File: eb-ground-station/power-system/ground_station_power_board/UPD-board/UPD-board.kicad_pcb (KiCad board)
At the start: 2 copper layers, 140.7 x 86.5 mm, 171 parts, among them J1 Conn_01x04, J10 PI 1827486, J2 PC 1720806, J3 Conn_01x03, J4 Conn_01x03, J5 Conn_01x03, J6 Conn_01x03, J7 PI 1924143, J8 PI 1827923, J9 PI 1827486, Q1 DMN61D8L-LVT, Q10 DMN61D8L-LVT, Q11 SUD50P08-25L-E3, Q12 SUD50P08-25L-E3, Q13 DMN61D8L-LVT, Q14 DMN61D8L-LVT, Q15 DMN61D8L-LVT, Q16 SUD50P08-25L-E3, Q17 SUD50P08-25L-E3, Q18 DMN61D8L-LVT, Q19 SUD50P08-25L-E3, Q2 DMN61D8L-LVT, Q20 SUD50P08-25L-E3, Q21 SUD50P08-25L-E3, Q22 SUD50P08-25L-E3, Q3 DMN61D8L-LVT, Q4 SUD50P08-25L-E3, Q5 SUD50P08-25L-E3, Q6 DMN61D8L-LVT, Q7 DMN61D8L-LVT, Q8 DMN61D8L-LVT, Q9 DMN61D8L-LVT, U1 MAX7310ATE, U10 TC4427, U11 TC4427, U12 TC4427, U13 TC4427, U14 TC4427, U15 TC4427, U16 TC4427, U17 TC4427, U18 TC4427, U19 TC4427, U2 MAX7310ATE, U3 MAX7310ATE, U4 MCP9808, U5 ADS1115IDGS, U6 UA78M33, U7 U_RasPi_40pin, U8 TC4427, U9 TC4427

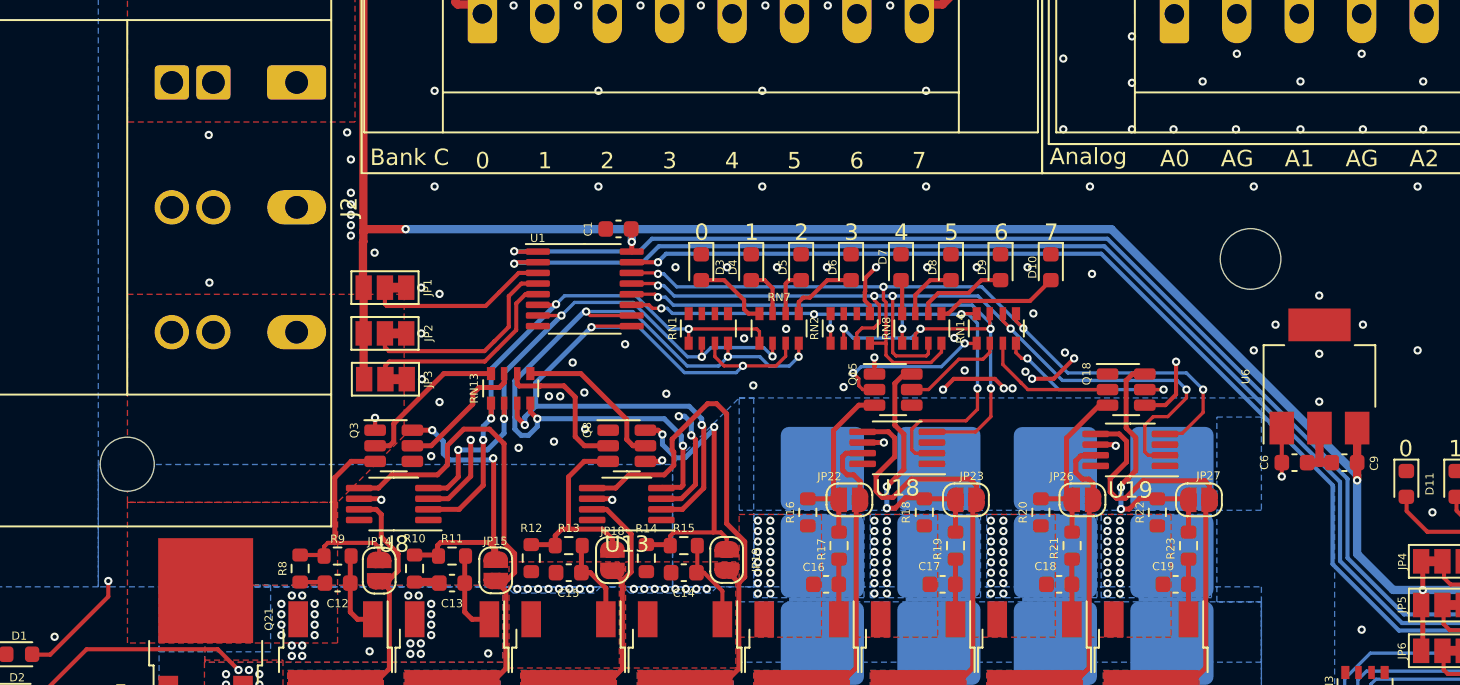
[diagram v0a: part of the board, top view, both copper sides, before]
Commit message: Upgrading Bank A to 16A
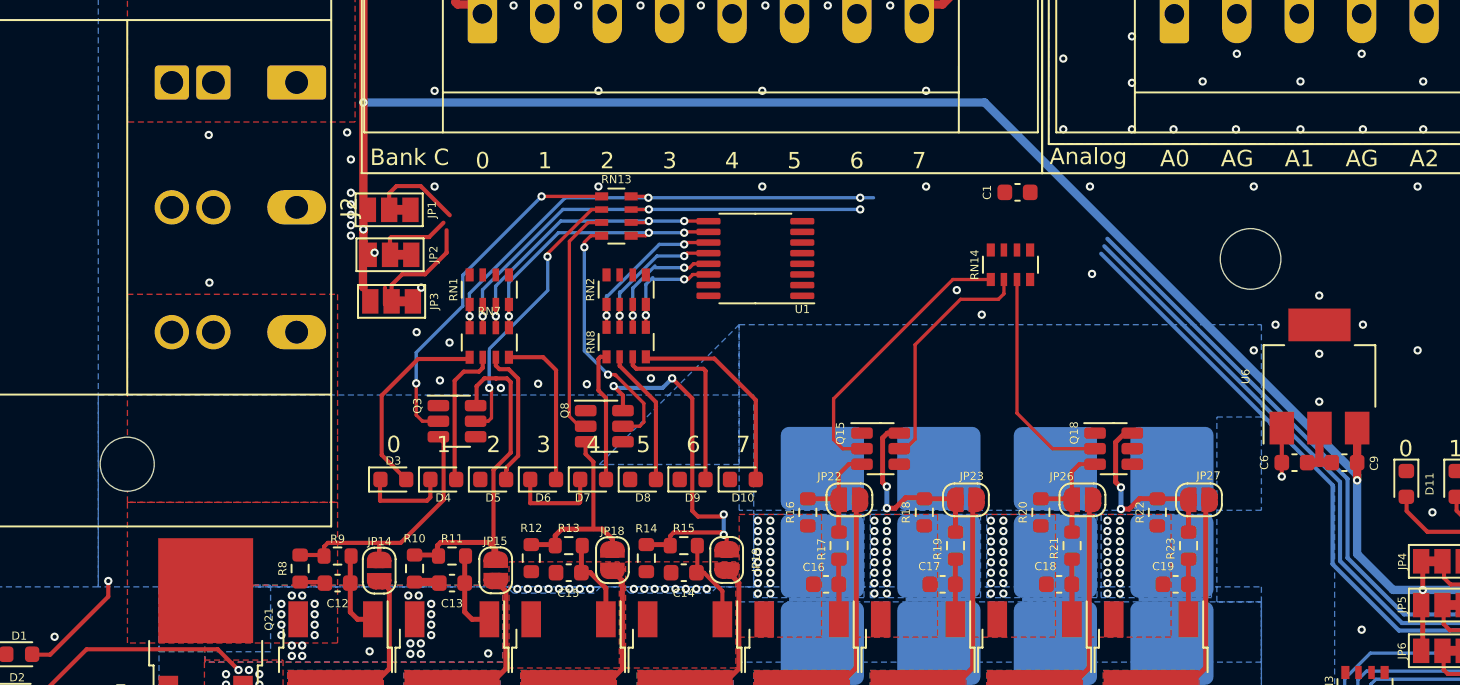
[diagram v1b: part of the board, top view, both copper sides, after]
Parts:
- removed U13, U18, U19, U8: TC4427, Package_SO:MSOP-8_3x3mm_P0.65mm
- moved C1 24.5 mm to (146.7, 88.9)
- moved D3 22.8 mm to (108.6, 106.4), turned to 0 degrees
- moved D8 22.8 mm to (123.9, 106.4), turned to 0 degrees
- moved D10 22.8 mm to (129.9, 106.4), turned to 0 degrees
- moved D4 22.8 mm to (111.7, 106.4), turned to 0 degrees
- moved D5 22.8 mm to (114.7, 106.4), turned to 0 degrees
- moved D6 22.8 mm to (117.8, 106.4), turned to 0 degrees
- moved D7 22.8 mm to (120.8, 106.4), turned to 0 degrees
- moved D9 22.8 mm to (126.9, 106.4), turned to 0 degrees
- moved RN8 18.1 mm to (122.8, 98.0)
- moved RN7 17.7 mm to (114.5, 98.0)
- moved RN2 13.9 mm to (122.8, 94.8)
- moved RN1 13.6 mm to (114.5, 94.8)
- moved RN13 12.3 mm to (122.2, 90.3), turned to 180 degrees
- moved U1 10.6 mm to (130.7, 92.9), turned to 180 degrees
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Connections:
- RN13 pad 1: MOS_A3 -> CTL_A3
- RN13 pad 2: MOS_A2 -> CTL_A2
- RN13 pad 3: MOS_A1 -> CTL_A1
- RN13 pad 4: MOS_A0 -> CTL_A0
- RN13 pad 5: CTL_A0 -> MOS_A0
- RN13 pad 6: CTL_A1 -> MOS_A1
- RN13 pad 7: CTL_A2 -> MOS_A2
- RN13 pad 8: CTL_A3 -> MOS_A3
- RN7 pad 1: Net-(D6-Pad2) -> CTL_A3
- RN7 pad 2: Net-(D5-Pad2) -> CTL_A2
- RN7 pad 3: Net-(D4-Pad2) -> CTL_A1
- RN7 pad 4: Net-(D3-Pad2) -> CTL_A0
- RN7 pad 5: CTL_A0 -> Net-(D3-Pad2)
- RN7 pad 6: CTL_A1 -> Net-(D4-Pad2)
- RN7 pad 7: CTL_A2 -> Net-(D5-Pad2)
- RN7 pad 8: CTL_A3 -> Net-(D6-Pad2)
- RN8 pad 1: Net-(D10-Pad2) -> CTL_A7
- RN8 pad 2: Net-(D9-Pad2) -> CTL_A6
- RN8 pad 3: Net-(D8-Pad2) -> CTL_A5
- RN8 pad 4: Net-(D7-Pad2) -> CTL_A4
- RN8 pad 5: CTL_A4 -> Net-(D7-Pad2)
- RN8 pad 6: CTL_A5 -> Net-(D8-Pad2)
- RN8 pad 7: CTL_A6 -> Net-(D9-Pad2)
- RN8 pad 8: CTL_A7 -> Net-(D10-Pad2)
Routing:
- net CTL_A6: track 54.8 -> 8.37 mm, vias 5 -> 2
- net CTL_A7: track 52.8 -> 7.42 mm, vias 4 -> 2
- net SCL: track 238.9 -> 201.0 mm, vias 6 -> 5
- net SDA: track 233.7 -> 195.9 mm, vias 6 -> 5
- net CTL_A5: track 44.6 -> 9.32 mm, vias 5 -> 2
- net ~{IO_RESET}: track 216.1 -> 187.3 mm, vias 5 -> 4
- net CTL_A4: track 38.5 -> 10.2 mm, vias 6 -> 2
- net CTL_A3: track 45.7 -> 18.1 mm, vias 5 -> 3
- net CTL_A2: track 46.5 -> 19.0 mm, vias 4 -> 3
- net OUT_A3: track 33.5 -> 10.9 mm
- net OUT_A1: track 31.2 -> 10.9 mm
- net GND: track 133.6 -> 114.8 mm, vias 255 -> 221
- net OUT_A5: track 28.7 -> 15.1 mm
- net OUT_A7: track 28.2 -> 14.9 mm
- net MOS_A0: track 9.54 -> 21.8 mm, vias 0 -> 2
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
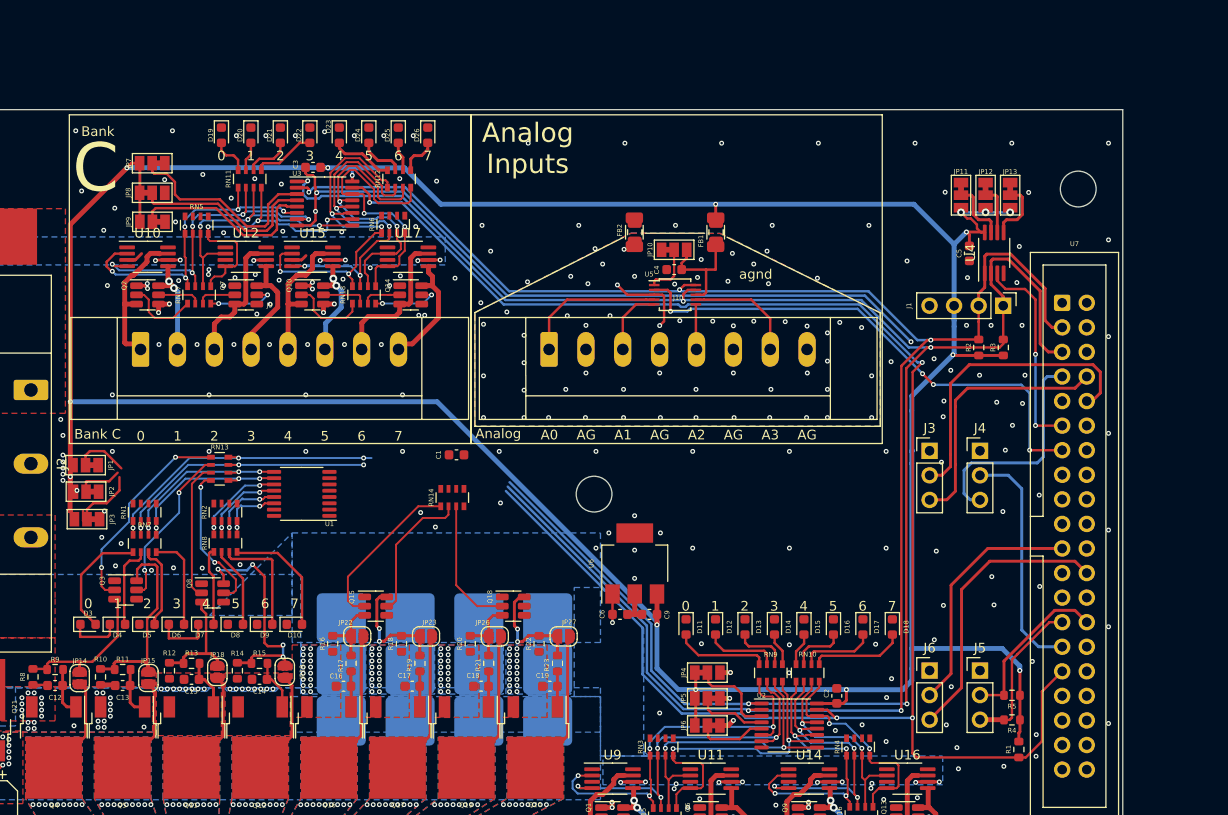
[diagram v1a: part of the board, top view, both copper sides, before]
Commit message: Finished routing with higher current traces
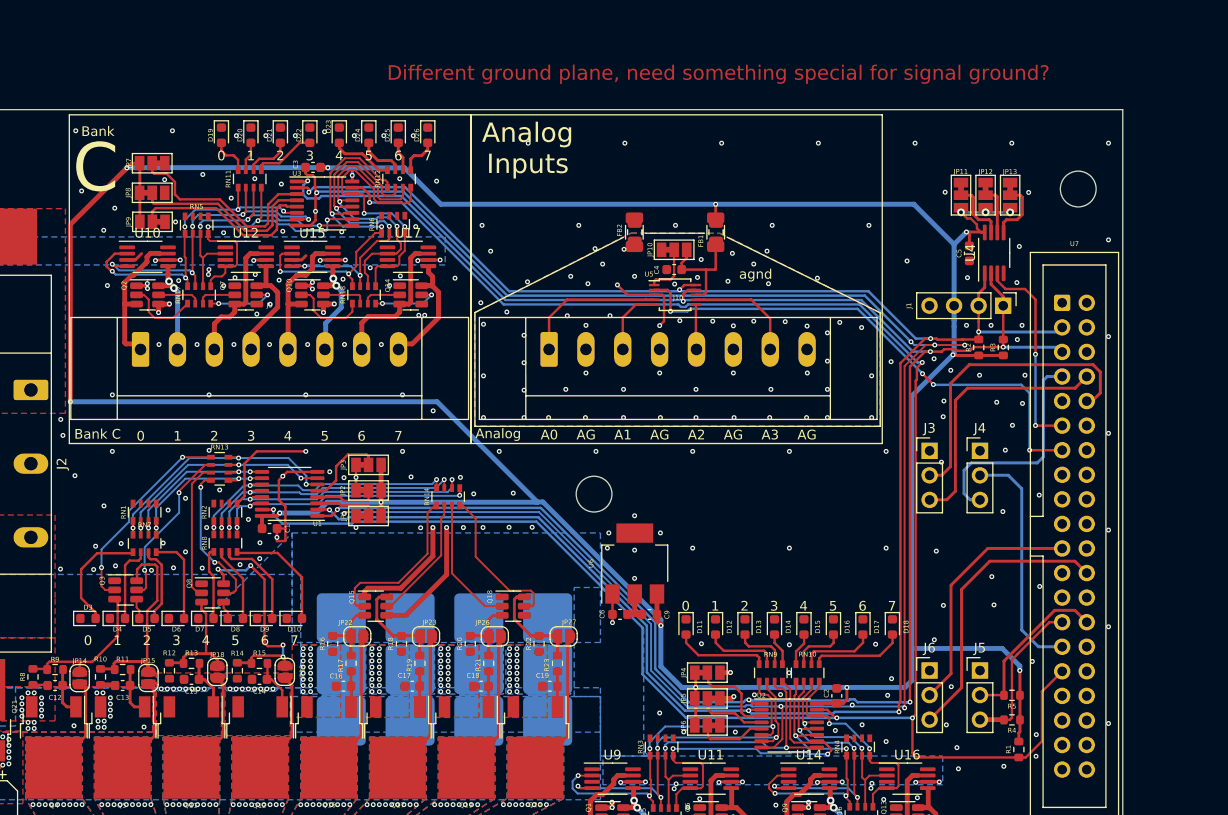
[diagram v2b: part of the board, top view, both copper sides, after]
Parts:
- moved JP1 29.7 mm to (137.6, 95.2), turned to 0 degrees
- moved JP3 29.6 mm to (137.6, 89.9), turned to 0 degrees
- moved JP2 29.2 mm to (137.6, 92.6), turned to 0 degrees
- moved C1 20.8 mm to (127.4, 96.5), turned to 0 degrees
- moved U1 1.24 mm to (129.5, 92.9)
- moved D10 0.61 mm to (129.9, 105.8)
- moved D3 0.61 mm to (108.6, 105.8)
- moved D4 0.61 mm to (111.7, 105.8)
- moved D5 0.61 mm to (114.7, 105.8)
- moved D6 0.61 mm to (117.8, 105.8)
- moved D7 0.61 mm to (120.8, 105.8)
- moved D8 0.61 mm to (123.9, 105.8)
- moved D9 0.61 mm to (126.9, 105.8)
- moved RN14 0.44 mm to (145.8, 93.2)
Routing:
- net GND: track 114.8 -> 279.4 mm, vias 221 -> 252
- net ~{IO_RESET}: track 187.3 -> 212.2 mm, vias 4 -> 5
- net CTL_A6: track 8.37 -> 30.1 mm, vias 2 -> 3
- net CTL_A7: track 7.42 -> 29.0 mm, vias 2 -> 3
- net CTL_A5: track 9.32 -> 29.7 mm, vias 2 -> 3
- net CTL_A4: track 10.2 -> 29.8 mm, vias 2 -> 3
- net MOS_A7: track 0.00 -> 16.0 mm
- net SDA: track 195.9 -> 209.0 mm, vias 5 -> 7
- net SCL: track 201.0 -> 211.1 mm, vias 5 -> 7
- net +3V3: track 377.6 -> 385.2 mm, vias 15 -> 16
- net CTL_B3: track 34.0 -> 40.9 mm
- net CTL_A1: track 29.4 -> 25.0 mm
- net CTL_A0: track 31.0 -> 27.1 mm
- net Net-(JP2-Pad2): track 4.66 -> 6.49 mm
- net Net-(D9-Pad2): track 11.7 -> 9.97 mm
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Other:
- board text added: "Different ground plane, need something special for signal ground?"

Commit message: Silkscreen almost done
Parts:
- added D3: LED, LED_SMD:LED_0603_1608Metric, F.Cu at (84.3, 122.1)
- added J11: Conn_02x02_Odd_Even, Connector_PinHeader_2.54mm:PinHeader_2x02_P2.54mm_Vertical, F.Cu at (201.3, 84.8)
- added R27: 4k7, Resistor_SMD:R_0603_1608Metric, F.Cu at (204.9, 67.9)
- added R28: 4k7, Resistor_SMD:R_0603_1608Metric, F.Cu at (204.7, 89.2)
- added R8: 1500, Resistor_SMD:R_0603_1608Metric, F.Cu at (81.2, 122.1)
- added TP1: TestPoint, oresat-footprints:TestPoint_Pad_1.5x1.5mm, F.Cu at (87.2, 117.1)
- added TP2: TestPoint, oresat-footprints:TestPoint_Pad_1.5x1.5mm, F.Cu at (87.2, 119.6)
- added TP3: TestPoint, oresat-footprints:TestPoint_Pad_1.5x1.5mm, F.Cu at (87.2, 122.1)
- moved JP13 5.10 mm to (198.9, 62.0)
- moved JP11 5.08 mm to (204.0, 62.0)
- moved D1 1.40 mm to (84.4, 117.1)
- moved D2 1.40 mm to (84.3, 119.6)
- moved R6 1.40 mm to (81.3, 117.1)
- moved R7 1.40 mm to (81.2, 119.6)
- moved J3 1.28 mm to (195.6, 89.7)
- moved J4 1.28 mm to (200.8, 89.7)
- moved R25 1.10 mm to (94.7, 62.0), turned to 180 degrees
- moved D10 0.46 mm to (126.9, 106.2)
- moved D11 0.46 mm to (129.9, 106.2)
- moved D4 0.46 mm to (108.6, 106.2)
- moved D5 0.46 mm to (111.7, 106.2)
- moved D6 0.46 mm to (114.7, 106.2)
- moved D7 0.46 mm to (117.8, 106.2)
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- renumbered C15 to C14, C14 to C15, D9 to D10, D10 to D11, D11 to D12, D12 to D13, D13 to D14, D14 to D15, D15 to D16, D16 to D17, D17 to D18, D18 to D19, D19 to D20, D20 to D21, D21 to D22, D22 to D23, D23 to D24, D24 to D25, D25 to D26, D26 to D27, D3 to D4, D4 to D5, D5 to D6, D6 to D7, D7 to D8, D8 to D9, R9 to R10, R10 to R11, R11 to R12, R12 to R13, R13 to R14, R14 to R15, R15 to R16, R16 to R17, R17 to R18, R18 to R19, R19 to R20, R20 to R21, R21 to R22, R22 to R23, R23 to R26, R8 to R9
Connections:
- JP1 pad 1: GND -> SCL
- JP1 pad 3: +3V3 -> SDA
- JP2 pad 1: GND -> SCL
- JP2 pad 3: +3V3 -> SDA
- JP3 pad 1: GND -> SCL
- JP3 pad 3: +3V3 -> SDA
- JP4 pad 1: +3V3 -> SDA
- JP4 pad 3: GND -> SCL
- JP5 pad 1: GND -> SCL
- JP5 pad 3: +3V3 -> SDA
- JP6 pad 1: GND -> SCL
- JP6 pad 3: +3V3 -> SDA
- JP7 pad 1: GND -> SCL
- JP7 pad 3: +3V3 -> SDA
- JP8 pad 1: +3V3 -> SDA
- JP8 pad 3: GND -> SCL
- JP9 pad 1: GND -> SCL
- JP9 pad 3: +3V3 -> SDA
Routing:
- net +3V3: track 385.2 -> 442.0 mm, vias 16 -> 15
- net SDA: track 209.0 -> 253.7 mm, vias 7 -> 14
- net SCL: track 211.1 -> 254.1 mm, vias 7 -> 9
- net TMP_ALERT: track 21.3 -> 32.2 mm
- net ~{IO_RESET}: track 212.2 -> 217.4 mm, vias 5 -> 6
- net GND: track 279.4 -> 275.5 mm, vias 252 -> 259
- net TX0: track 27.0 -> 30.1 mm
- net Net-(JP11-Pad2): track 6.41 -> 8.98 mm, vias 0 -> 2
- net ADC_RDY: track 53.8 -> 56.2 mm
- net Net-(JP13-Pad2): track 6.45 -> 8.59 mm, vias 0 -> 2
- net Net-(JP5-Pad2): track 7.10 -> 9.17 mm
- net CTL_A0: track 27.1 -> 28.9 mm
- net +12V: track 28.5 -> 30.2 mm
- net Net-(D3-Pad1): track 0.00 -> 1.44 mm
- net +5V: track 21.5 -> 22.9 mm
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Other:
- board text added: "(internal)"
- board text added: "0011xxx"
- board text added: "0100xxx"
- board text added: "0x18 →0x1F"
- board text added: "0x20 →0x27"
- board text added: "0x20→0x27"
- board text added: "0x48"
- board text added: "0x49"
- board text added: "12V"
- board text added: "12V Max 16A 5V Max 16A 3.3V Max 1A"
- board text added: "12v"
- board text added: "2022-09-xx"
- board text added: "3.3V"
- board text added: "3.3V reg"
- board text added: "39"
- board text added: "40"
- board text added: "5V"
- board text added: "5v"
- board text added: "A"
- board text added: "AD0"
- board text added: "AD1"
- board text added: "AD2"
- board text added: "ADC Rdy"
- board text added: "Addr."
- board text added: "B"
- board text added: "Bank A"
- board text added: "Bank B"
- board text added: "C0"
- board text added: "C1"
- board text added: "GND 3.3V SDA SCL"
- board text added: "I"
- board text added: "IO Reset"
- board text added: "Power"
- board text added: "RasPi"
- board text added: "Rename ADC_READY and TMP_ALERT to active low names"
- board text added: "Rev. 2"
- board text added: "SCL"
- board text added: "SDA"
- board text added: "Temp. Sensor"
- board text added: "Tmp Alrt"
- board text added: "UART0"
- board text added: "UART2"
- board text added: "UART3"
- board text added: "UART4"
- board text added: "UARTx"
- board text added: "Uniclogs Power Board"
- board text added: "alt:"
- board text added: "gnd"
- board text added: "rx (in)"
- board text added: "tx (out)"
- board text removed: "Try to move stuff further from large parts"

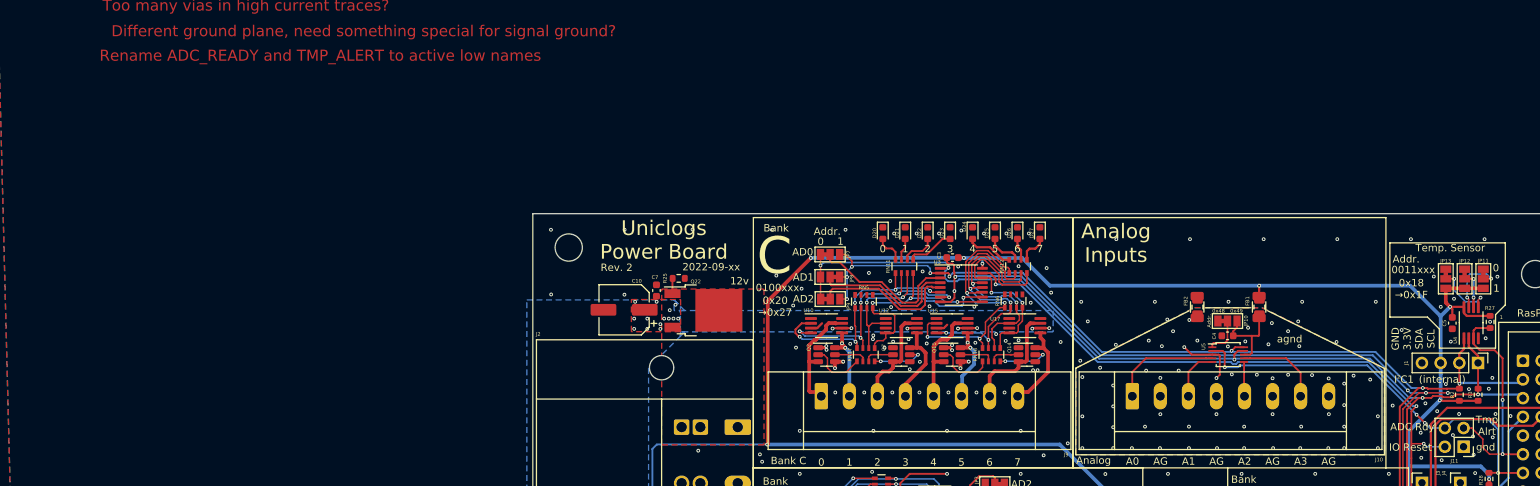
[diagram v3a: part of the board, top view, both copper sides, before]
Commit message: Made new drawings and renders
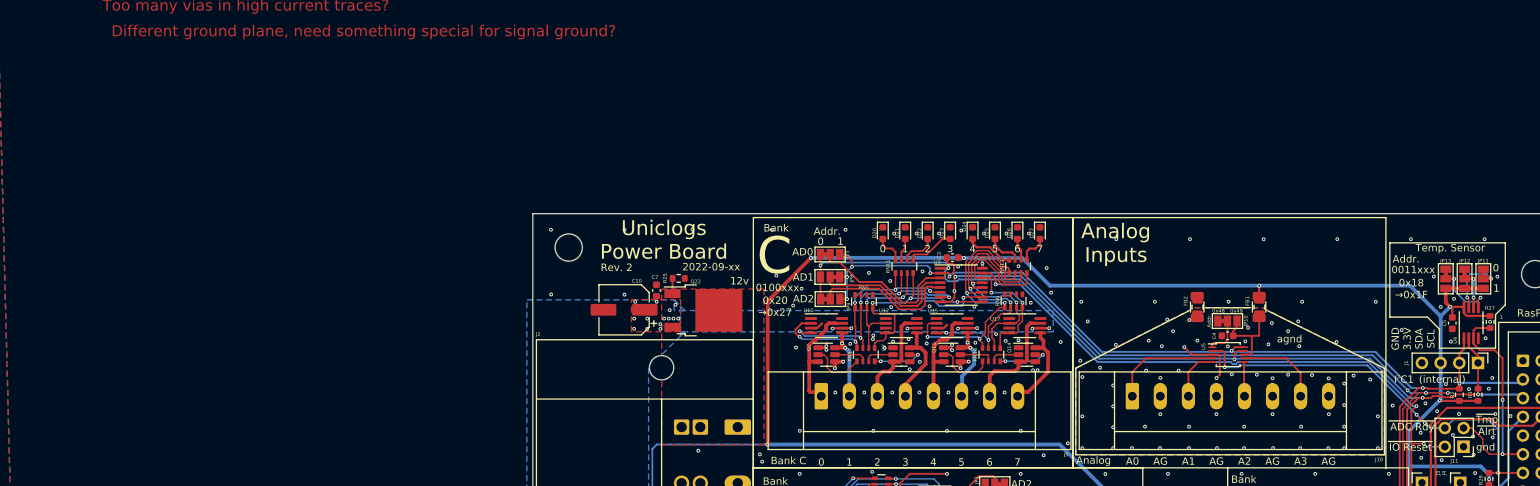
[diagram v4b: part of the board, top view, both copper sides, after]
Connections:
- net ADC_RDY renamed ~{ADC_RDY}
- net TMP_ALERT renamed ~{TMP_ALERT}
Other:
- board text added: "A4"
- board text added: "A5"
- board text added: "A6"
- board text added: "A7"
- board text removed: "Rename ADC_READY and TMP_ALERT to active low names"
